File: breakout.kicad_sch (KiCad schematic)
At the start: 36 parts, among them J1 16PIN, J2 CV_IN, J3 GATE_IN, J4 POWER_IN

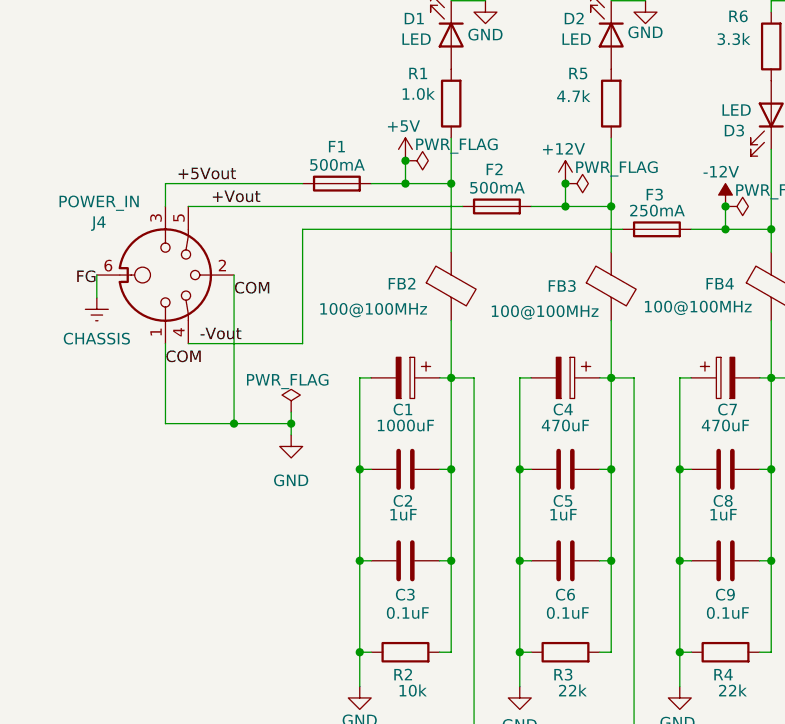
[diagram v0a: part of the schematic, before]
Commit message: update power symobl
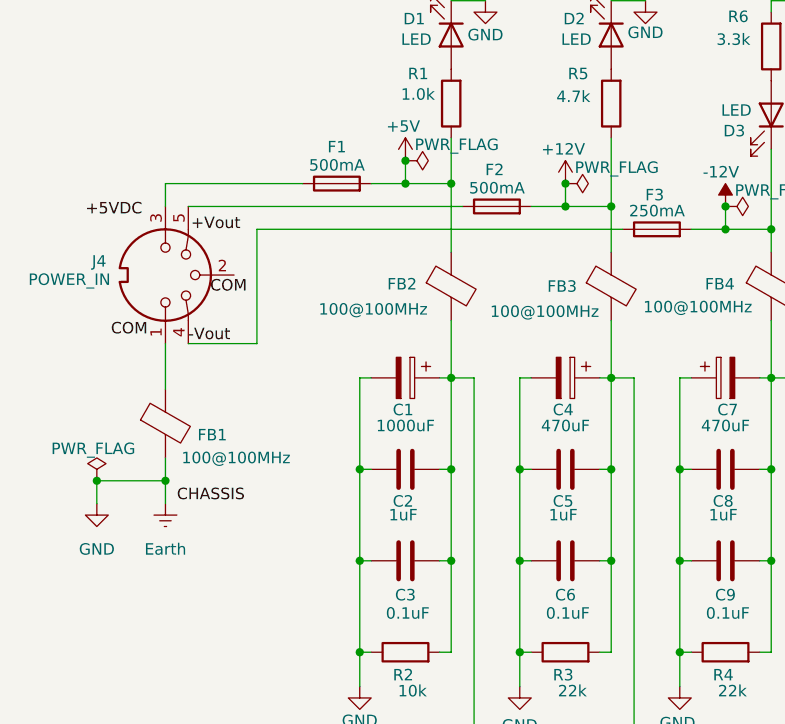
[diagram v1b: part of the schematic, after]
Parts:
- added FB1: 100@100MHz, Inductor_THT:L_Axial_L5.3mm_D2.2mm_P7.62mm_Horizontal_Vishay_IM-1, symbol Device:FerriteBead
- J4: symbol drichert:MeanWell-GP25A-DIN-5_180degree -> Connector:DIN-5_180degree
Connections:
- net +Vout: no longer F2.1, J4.5 (+12V)
- net CHASSIS: no longer J4.6 (FG)
- net +5Vout: no longer names the net of F1.1, J4.3
- net GND renamed Earth
- net Earth: now also FB1.2; no longer J4.1 (COM), J4.2 (COM)
- new net: F2.1, J4.5
- new net: FB1.1, J4.1
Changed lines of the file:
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@@
 	)
 	(junction
-		(at 63.5 88.9)
-		(diameter 0)
-		(color 0 0 0 0)
-	)
-	(junction
 		(at 95.25 93.98)
 		(diameter 0)
@@
 	)
 	(junction
-		(at 69.85 88.9)
-		(diameter 0)
-		(color 0 0 0 0)
-	)
-	(junction
 		(at 78.74 163.83)
 		(diameter 0)
@@
 	)
 	(junction
+		(at 48.26 95.25)
+		(diameter 0)
+		(color 0 0 0 0)
+	)
+	(junction
 		(at 123.19 67.31)
 		(diameter 0)
@@
 	)
 	(junction
+		(at 55.88 95.25)
+		(diameter 0)
+		(color 0 0 0 0)
+	)
+	(junction
 		(at 95.25 104.14)
 		(diameter 0)
@@
 	(wire
 		(pts
+			(xy 55.88 95.25) (xy 55.88 92.71)
+		)
+		(stroke
+			(width 0)
+			(type default)
+		)
+	)
+	(wire
+		(pts
 			(xy 123.19 139.7) (xy 123.19 152.4)
 		)
@@
 	(wire
 		(pts
-			(xy 71.12 67.31) (xy 106.68 67.31)
+			(xy 66.04 67.31) (xy 106.68 67.31)
 		)
 		(stroke
@@
 	(wire
 		(pts
-			(xy 71.12 80.01) (xy 71.12 67.31)
+			(xy 66.04 80.01) (xy 66.04 67.31)
 		)
 		(stroke
@@
 	(wire
 		(pts
-			(xy 63.5 72.39) (xy 63.5 88.9)
-		)
-		(stroke
-			(width 0)
-			(type default)
-		)
-	)
-	(wire
-		(pts
 			(xy 118.11 67.31) (xy 123.19 67.31)
 		)
@@
 	(wire
 		(pts
-			(xy 69.85 88.9) (xy 69.85 90.17)
-		)
-		(stroke
-			(width 0)
-			(type default)
-		)
-	)
-	(wire
-		(pts
-			(xy 55.88 88.9) (xy 63.5 88.9)
+			(xy 55.88 95.25) (xy 48.26 95.25)
 		)
 		(stroke
@@
 	(wire
 		(pts
-			(xy 69.85 87.63) (xy 69.85 88.9)
+			(xy 48.26 95.25) (xy 48.26 97.79)
 		)
 		(stroke
@@
 	(wire
 		(pts
-			(xy 55.88 80.01) (xy 55.88 88.9)
-		)
-		(stroke
-			(width 0)
-			(type default)
-		)
-	)
-	(wire
-		(pts
 			(xy 63.5 144.78) (xy 74.93 144.78)
 		)
@@
 	(wire
 		(pts
-			(xy 48.26 72.39) (xy 48.26 74.93)
-		)
-		(stroke
-			(width 0)
-			(type default)
-		)
-	)
-	(wire
-		(pts
 			(xy 95.25 114.3) (xy 95.25 118.11)
 		)
@@
 	(wire
 		(pts
-			(xy 58.42 80.01) (xy 71.12 80.01)
+			(xy 58.42 80.01) (xy 66.04 80.01)
 		)
 		(stroke
@@
 	(wire
 		(pts
+			(xy 55.88 80.01) (xy 55.88 85.09)
+		)
+		(stroke
+			(width 0)
+			(type default)
+		)
+	)
+	(wire
+		(pts
 			(xy 115.57 128.27) (xy 115.57 139.7)
 		)
@@
 	(wire
 		(pts
+			(xy 55.88 95.25) (xy 55.88 97.79)
+		)
+		(stroke
+			(width 0)
+			(type default)
+		)
+	)
+	(wire
+		(pts
 			(xy 77.47 83.82) (xy 77.47 93.98)
 		)
@@
 	(wire
 		(pts
-			(xy 63.5 88.9) (xy 69.85 88.9)
-		)
-		(stroke
-			(width 0)
-			(type default)
-		)
-	)
-	(wire
-		(pts
 			(xy 92.71 163.83) (xy 97.79 163.83)
 		)
@@
 		)
 	)
-	(label "+5Vout"
-		(at 57.15 62.23 0)
+	(label "CHASSIS"
+		(at 57.15 97.79 0)
 		(effects
 			(font
@@
 	)
 	(label "+Vout"
-		(at 60.96 64.77 0)
+		(at 58.718 67.6652 0)
 		(effects
 			(font
@@
 	)
 	(label "COM"
-		(at 55.88 82.55 0)
+		(at 49.8194 79.3739 0)
 		(effects
 			(font
@@
 	)
 	(label "COM"
-		(at 63.5 74.93 0)
+		(at 60.8468 74.6053 0)
 		(effects
 			(font
@@
 		)
 	)
-	(label "-Vout"
-		(at 59.69 80.01 0)
+	(label "+5VDC"
+		(at 46.99 66.04 0)
 		(effects
 			(font
@@
 		)
 	)
-	(label "FG"
-		(at 48.26 73.66 180)
+	(label "-Vout"
+		(at 58.42 80.01 0)
 		(effects
 			(font
 				(size 1.27 1.27)
 			)
-			(justify right bottom)
+			(justify left bottom)
 		)
 	)
@@
 	(symbol
 		(lib_id "power:Earth")
-		(at 48.26 74.93 0)
-		(mirror y)
+		(at 55.88 97.79 0)
 		(unit 1)
 		(exclude_from_sim no)
@@
 		(on_board yes)
 		(dnp no)
+		(fields_autoplaced yes)
 		(property "Reference" "#PWR05"
-			(at 48.26 81.28 0)
+			(at 55.88 104.14 0)
 			(effects
 				(font
@@
 			)
 		)
-		(property "Value" "CHASSIS"
-			(at 48.26 79.502 0)
+		(property "Value" "Earth"
+			(at 55.88 102.87 0)
 			(effects
 				(font
@@
 		)
 		(property "Footprint" ""
-			(at 48.26 74.93 0)
+			(at 55.88 97.79 0)
 			(effects
 				(font
@@
 		)
 		(property "Datasheet" "~"
-			(at 48.26 74.93 0)
+			(at 55.88 97.79 0)
 			(effects
 				(font
@@
 		)
 		(property "Description" "Power symbol creates a global label with name \"Earth\""
-			(at 48.26 74.93 0)
+			(at 55.88 97.79 0)
 			(effects
 				(font
@@
 		)
 		(instances
-			(project "bench-power"
+			(project ""
 				(path "/7d945acc-eebf-4bd3-96a2-bce5a0d85bfc"
 					(reference "#PWR05")
@@
 	(symbol
 		(lib_id "power:GND")
-		(at 69.85 90.17 0)
+		(at 48.26 97.79 0)
 		(unit 1)
 		(exclude_from_sim no)
@@
 		(dnp no)
 		(property "Reference" "#PWR011"
-			(at 69.85 96.52 0)
+			(at 48.26 104.14 0)
 			(effects
 				(font
@@
 		)
 		(property "Value" "GND"
-			(at 69.85 95.25 0)
+			(at 48.26 102.87 0)
 			(effects
 				(font
@@
 		)
 		(property "Footprint" ""
-			(at 69.85 90.17 0)
+			(at 48.26 97.79 0)
 			(effects
 				(font
@@
 		)
 		(property "Datasheet" ""
-			(at 69.85 90.17 0)
+			(at 48.26 97.79 0)
 			(effects
 				(font
@@
 		)
 		(property "Description" "Power symbol creates a global label with name \"GND\" , ground"
-			(at 69.85 90.17 0)
+			(at 48.26 97.79 0)
 			(effects
 				(font
@@
 	(symbol
 		(lib_id "power:PWR_FLAG")
-		(at 69.85 87.63 0)
+		(at 48.26 95.25 0)
 		(unit 1)
 		(exclude_from_sim no)
@@
 		(dnp no)
 		(property "Reference" "#FLG04"
-			(at 69.85 85.725 0)
+			(at 48.26 93.345 0)
 			(effects
 				(font
@@
 		)
 		(property "Value" "PWR_FLAG"
-			(at 64.77 84.074 0)
+			(at 43.18 91.694 0)
 			(effects
 				(font
@@
 		)
 		(property "Footprint" ""
-			(at 69.85 87.63 0)
+			(at 48.26 95.25 0)
 			(effects
 				(font
@@
 		)
 		(property "Datasheet" "~"
-			(at 69.85 87.63 0)
+			(at 48.26 95.25 0)
 			(effects
 				(font
@@
 		)
 		(property "Description" "Special symbol for telling ERC where power comes from"
-			(at 69.85 87.63 0)
+			(at 48.26 95.25 0)
 			(effects
 				(font
@@
 	)
 	(symbol
+		(lib_id "Device:FerriteBead")
+		(at 55.88 88.9 0)
+		(unit 1)
+		(exclude_from_sim no)
+		(in_bom yes)
+		(on_board yes)
+		(dnp no)
+		(property "Reference" "FB1"
+			(at 59.436 90.17 0)
+			(effects
+				(font
+					(size 1.27 1.27)
+				)
+				(justify left)
+			)
+		)
+		(property "Value" "100@100MHz"
+			(at 57.658 92.71 0)
+			(effects
+				(font
+					(size 1.27 1.27)
+				)
+				(justify left)
+			)
+		)
+		(property "Footprint" "Inductor_THT:L_Axial_L5.3mm_D2.2mm_P7.62mm_Horizontal_Vishay_IM-1"
+			(at 54.102 88.9 90)
+			(effects
+				(font
+					(size 1.27 1.27)
+				)
+				(hide yes)
+			)
+		)
+		(property "Datasheet" "~"
+			(at 55.88 88.9 0)
+			(effects
+				(font
+					(size 1.27 1.27)
+				)
+				(hide yes)
+			)
+		)
+		(property "Description" "Ferrite bead"
+			(at 55.88 88.9 0)
+			(effects
+				(font
+					(size 1.27 1.27)
+				)
+				(hide yes)
+			)
+		)
+		(pin "2"
+		)
+		(pin "1"
+		)
+		(instances
+			(project ""
+				(path "/7d945acc-eebf-4bd3-96a2-bce5a0d85bfc"
+					(reference "FB1")
+					(unit 1)
+				)
+			)
+		)
+	)
+	(symbol
 		(lib_id "Device:R")
 		(at 82.55 114.3 90)
@@
 	)
 	(symbol
-		(lib_id "drichert:MeanWell-GP25A-DIN-5_180degree")
+		(lib_id "Connector:DIN-5_180degree")
 		(at 55.88 72.39 270)
 		(mirror x)
@@
 		(dnp no)
 		(property "Reference" "J4"
-			(at 48.514 66.548 90)
+			(at 48.514 70.866 90)
 			(effects
 				(font
@@
 		)
 		(property "Value" "POWER_IN"
-			(at 48.514 64.262 90)
+			(at 45.212 72.898 90)
 			(effects
 				(font
@@
 		(pin "2"
 		)
-		(pin "6"
-		)
 		(instances
